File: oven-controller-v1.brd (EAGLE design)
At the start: 160 x 100 mm, 21 parts, among them Q1 IRFL310, U1 ARDUINO_SHIELDLONGPADS

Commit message: All parts on the board, cleaned up layout.
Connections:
- net 5V: now also U1.5V
- net A0: now also U1.A0
- net A1: now also U1.A1
- net A2: now also U1.A2
- net A3: now also U1.A3
- net CS_PIN10: now also U1.D10
- net CS_PIN5: now also U1.D5
- net CS_PIN6: now also U1.D6
- net CS_PIN7: now also U1.D7
- net CS_PIN8: now also U1.D8
- net CS_PIN9: now also U1.D9
- net GND: now also U1.GND@0, U1.GND@1, U1.GND@2
- net PIN12: now also U1.D12
- net SCLK_PIN4: now also U1.D4
- net SDA_PIN3: now also U1.D3
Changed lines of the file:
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@@
 <contactref element="ROTATESW" pad="4"/>
 <contactref element="LED1" pad="K"/>
-<wire x1="-71.12" y1="80.01" x2="-74.93" y2="-4.826" width="0" layer="19" extent="1-1"/>
+<contactref element="U1" pad="GND@2"/>
+<contactref element="U1" pad="GND@1"/>
+<contactref element="U1" pad="GND@0"/>
+<wire x1="25.654" y1="50.8" x2="28.194" y2="50.8" width="0" layer="19" extent="1-1"/>
+<wire x1="42.164" y1="2.54" x2="28.194" y2="50.8" width="0" layer="19" extent="1-1"/>
+<wire x1="-16.51" y1="82.55" x2="25.654" y2="50.8" width="0" layer="19" extent="1-1"/>
+<wire x1="-22.86" y1="88.9" x2="-16.51" y2="82.55" width="0" layer="19" extent="1-1"/>
+<wire x1="-22.86" y1="95.25" x2="-22.86" y2="88.9" width="0" layer="19" extent="1-1"/>
+<wire x1="-39.37" y1="95.25" x2="-22.86" y2="95.25" width="0" layer="19" extent="1-1"/>
+<wire x1="-39.37" y1="88.9" x2="-39.37" y2="95.25" width="0" layer="19" extent="1-1"/>
+<wire x1="-55.88" y1="88.9" x2="-39.37" y2="88.9" width="0" layer="19" extent="1-1"/>
+<wire x1="-58.42" y1="80.01" x2="-55.88" y2="88.9" width="0" layer="19" extent="1-1"/>
+<wire x1="-71.12" y1="80.01" x2="-58.42" y2="80.01" width="0" layer="19" extent="1-1"/>
 <wire x1="-72.39" y1="88.9" x2="-71.12" y2="80.01" width="0" layer="19" extent="1-1"/>
 <wire x1="-76.2" y1="95.25" x2="-72.39" y2="88.9" width="0" layer="19" extent="1-1"/>
-<wire x1="-58.42" y1="80.01" x2="-71.12" y2="80.01" width="0" layer="19" extent="1-1"/>
-<wire x1="-55.88" y1="88.9" x2="-58.42" y2="80.01" width="0" layer="19" extent="1-1"/>
-<wire x1="-39.37" y1="88.9" x2="-55.88" y2="88.9" width="0" layer="19" extent="1-1"/>
-<wire x1="-39.37" y1="95.25" x2="-39.37" y2="88.9" width="0" layer="19" extent="1-1"/>
-<wire x1="-22.86" y1="95.25" x2="-39.37" y2="95.25" width="0" layer="19" extent="1-1"/>
-<wire x1="-22.86" y1="88.9" x2="-22.86" y2="95.25" width="0" layer="19" extent="1-1"/>
-<wire x1="-16.51" y1="82.55" x2="-22.86" y2="88.9" width="0" layer="19" extent="1-1"/>
+<wire x1="-74.93" y1="-4.826" x2="-71.12" y2="80.01" width="0" layer="19" extent="1-1"/>
 </signal>
 <signal name="PIN12">
+<contactref element="U1" pad="D12"/>
 <contactref element="R2" pad="2"/>
 <contactref element="R1" pad="2"/>
 <wire x1="-63.5" y1="95.25" x2="-48.26" y2="95.25" width="0" layer="19" extent="1-1"/>
+<wire x1="37.084" y1="2.54" x2="-48.26" y2="95.25" width="0" layer="19" extent="1-1"/>
 </signal>
 <signal name="N$2">
@@
 <contactref element="SENSE5" pad="4"/>
 <contactref element="SENSE6" pad="4"/>
+<contactref element="U1" pad="D3"/>
 <wire x1="-20.32" y1="88.646" x2="-20.32" y2="94.996" width="0" layer="19" extent="1-1"/>
 <wire x1="-36.83" y1="94.996" x2="-20.32" y2="94.996" width="0" layer="19" extent="1-1"/>
@@
 <wire x1="-53.34" y1="88.646" x2="-36.83" y2="88.646" width="0" layer="19" extent="1-1"/>
 <wire x1="-69.85" y1="88.646" x2="-53.34" y2="88.646" width="0" layer="19" extent="1-1"/>
+<wire x1="12.954" y1="2.54" x2="-20.32" y2="88.646" width="0" layer="19" extent="1-1"/>
 </signal>
 <signal name="SCLK_PIN4">
@@
 <contactref element="SENSE5" pad="6"/>
 <contactref element="SENSE6" pad="6"/>
+<contactref element="U1" pad="D4"/>
 <wire x1="-15.24" y1="88.646" x2="-15.24" y2="94.996" width="0" layer="19" extent="1-1"/>
 <wire x1="-31.75" y1="94.996" x2="-15.24" y2="94.996" width="0" layer="19" extent="1-1"/>
@@
 <wire x1="-48.26" y1="88.646" x2="-31.75" y2="88.646" width="0" layer="19" extent="1-1"/>
 <wire x1="-64.77" y1="88.646" x2="-48.26" y2="88.646" width="0" layer="19" extent="1-1"/>
+<wire x1="15.494" y1="2.54" x2="-15.24" y2="88.646" width="0" layer="19" extent="1-1"/>
 </signal>
 <signal name="CS_PIN10">
 <contactref element="SENSE6" pad="5"/>
+<contactref element="U1" pad="D10"/>
+<wire x1="32.004" y1="2.54" x2="-34.29" y2="95.25" width="0" layer="19" extent="1-1"/>
 </signal>
 <signal name="N$1">
@@
 <signal name="CS_PIN6">
 <contactref element="SENSE2" pad="5"/>
+<contactref element="U1" pad="D6"/>
+<wire x1="20.574" y1="2.54" x2="-34.29" y2="88.9" width="0" layer="19" extent="1-1"/>
 </signal>
 <signal name="CS_PIN8">
 <contactref element="SENSE4" pad="5"/>
+<contactref element="U1" pad="D8"/>
+<wire x1="-67.31" y1="88.9" x2="26.924" y2="2.54" width="0" layer="19" extent="1-1"/>
 </signal>
 <signal name="CS_PIN7">
 <contactref element="SENSE3" pad="5"/>
+<contactref element="U1" pad="D7"/>
+<wire x1="23.114" y1="2.54" x2="-50.8" y2="88.9" width="0" layer="19" extent="1-1"/>
 </signal>
 <signal name="CS_PIN9">
 <contactref element="SENSE5" pad="5"/>
+<contactref element="U1" pad="D9"/>
+<wire x1="29.464" y1="2.54" x2="-17.78" y2="95.25" width="0" layer="19" extent="1-1"/>
 </signal>
 <signal name="CS_PIN5">
 <contactref element="SENSE1" pad="5"/>
+<contactref element="U1" pad="D5"/>
+<wire x1="18.034" y1="2.54" x2="-17.78" y2="88.9" width="0" layer="19" extent="1-1"/>
 </signal>
 <signal name="N$11">
@@
 <contactref element="R4" pad="1"/>
 <contactref element="JP1" pad="1"/>
-<wire x1="-36.83" y1="100.33" x2="-82.677" y2="-24.13" width="0" layer="19" extent="1-1"/>
+<contactref element="U1" pad="A0"/>
+<wire x1="18.034" y1="50.8" x2="-82.677" y2="-24.13" width="0" layer="19" extent="1-1"/>
+<wire x1="-36.83" y1="100.33" x2="18.034" y2="50.8" width="0" layer="19" extent="1-1"/>
 </signal>
 <signal name="N$10">
@@
 <contactref element="ROTATESW" pad="1"/>
 <contactref element="R10" pad="1"/>
+<contactref element="U1" pad="A1"/>
 <wire x1="-82.55" y1="-4.572" x2="-83.058" y2="-19.304" width="0" layer="19" extent="1-1"/>
+<wire x1="15.494" y1="50.8" x2="-82.55" y2="-4.572" width="0" layer="19" extent="1-1"/>
 </signal>
 <signal name="A2">
 <contactref element="ROTATESW" pad="2"/>
 <contactref element="R9" pad="1"/>
+<contactref element="U1" pad="A2"/>
 <wire x1="-80.01" y1="-4.826" x2="-83.058" y2="-14.732" width="0" layer="19" extent="1-1"/>
+<wire x1="12.954" y1="50.8" x2="-80.01" y2="-4.826" width="0" layer="19" extent="1-1"/>
 </signal>
 <signal name="A3">
 <contactref element="ROTATESW" pad="3"/>
 <contactref element="R8" pad="1"/>
+<contactref element="U1" pad="A3"/>
 <wire x1="-77.47" y1="-4.572" x2="-83.058" y2="-10.16" width="0" layer="19" extent="1-1"/>
+<wire x1="10.414" y1="50.8" x2="-77.47" y2="-4.572" width="0" layer="19" extent="1-1"/>
 </signal>
 <signal name="5V">
@@
 <contactref element="R4" pad="2"/>
 <contactref element="R3" pad="2"/>
+<contactref element="U1" pad="5V"/>
 <wire x1="-72.898" y1="-14.732" x2="-72.898" y2="-19.304" width="0" layer="19" extent="1-1"/>
 <wire x1="-72.898" y1="-10.16" x2="-72.898" y2="-14.732" width="0" layer="19" extent="1-1"/>
@@
 <wire x1="-27.94" y1="88.9" x2="-27.94" y2="95.25" width="0" layer="19" extent="1-1"/>
 <wire x1="-13.97" y1="100.33" x2="-26.67" y2="100.33" width="0" layer="19" extent="1-1"/>
+<wire x1="30.734" y1="50.8" x2="-13.97" y2="100.33" width="0" layer="19" extent="1-1"/>
 </signal>
 <signal name="VIN">

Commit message: Schematic and layout done. Connections to Arduino will have to be female headers because we don't have plated vias.
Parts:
- removed JP1: (no value), SparkFun-Connectors:1X02_LOCK_LONGPADS
- added 12VIN, START: (no value), SparkFun-Connectors:SCREWTERMINAL-3.5MM-2_LOCK
- LED2: value GREEN -> RED
- R2: value (none) -> 10k
- RELAY: device SparkFun-Connectors:1X02_LOCK_LONGPADS -> SparkFun-Connectors:SCREWTERMINAL-3.5MM-2_LOCK
- moved RELAY 158.3 mm to (55.9, 18.5), turned to 90 degrees
- moved R2 141.7 mm to (45.5, 13.0), turned to 135 degrees
- moved LED2 128.5 mm to (52.6, 50.3), turned to 90 degrees
- moved SENSE4 121.5 mm to (24.6, 23.1), turned to 270 degrees
- moved R10 118.5 mm to (25.1, 39.1)
- moved R1 118.2 mm to (42.2, 27.4), turned to 270 degrees
- moved R9 114.4 mm to (25.1, 34.8)
- moved R8 110.7 mm to (25.1, 30.0)
- moved ROTATESW 109.3 mm to (15.0, 44.7), turned to 180 degrees
- moved SENSE6 108.9 mm to (37.1, 23.1), turned to 270 degrees
- moved D1 108.5 mm to (49.3, 19.3), turned to 90 degrees
- moved LED1 108.1 mm to (44.2, 50.3), turned to 90 degrees
- moved SENSE3 103.0 mm to (18.3, 23.1), turned to 270 degrees
- moved SENSE5 93.1 mm to (31.0, 23.1), turned to 270 degrees
- moved Q1 87.8 mm to (52.1, 33.5)
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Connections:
- removed net N$1: SENSE2.2
- removed net N$4: SENSE1.2
- removed net N$5: SENSE3.2
- removed net N$6: SENSE4.2
- removed net N$8: SENSE5.2
- removed net N$9: SENSE6.2
- net A0: now also START.1; no longer JP1.1
- net GND: now also 12VIN.2
- net N$10: now also START.2; no longer JP1.2
- net VIN: now also 12VIN.1
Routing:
- net 5V: track 0.00 -> 62.7 mm
- net A0: track 0.00 -> 55.9 mm
- net SDA_PIN3: track 0.00 -> 46.9 mm
- net SCLK_PIN4: track 0.00 -> 40.8 mm
- net CS_PIN5: track 0.00 -> 31.6 mm
- net A3: track 0.00 -> 25.2 mm
- net PIN12: track 0.00 -> 21.2 mm
- net A2: track 0.00 -> 20.4 mm
- net VIN: track 0.00 -> 17.3 mm
- net A1: track 0.00 -> 15.3 mm
- net N$3: track 0.00 -> 15.3 mm
- net CS_PIN6: track 0.00 -> 13.9 mm
- net CS_PIN10: track 0.00 -> 13.7 mm
- net CS_PIN9: track 0.00 -> 13.3 mm
- net CS_PIN7: track 0.00 -> 12.4 mm
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- added copper zone on layer 16, net GND
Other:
- board size 160 x 100 mm -> 159.5 x 103.6 mm

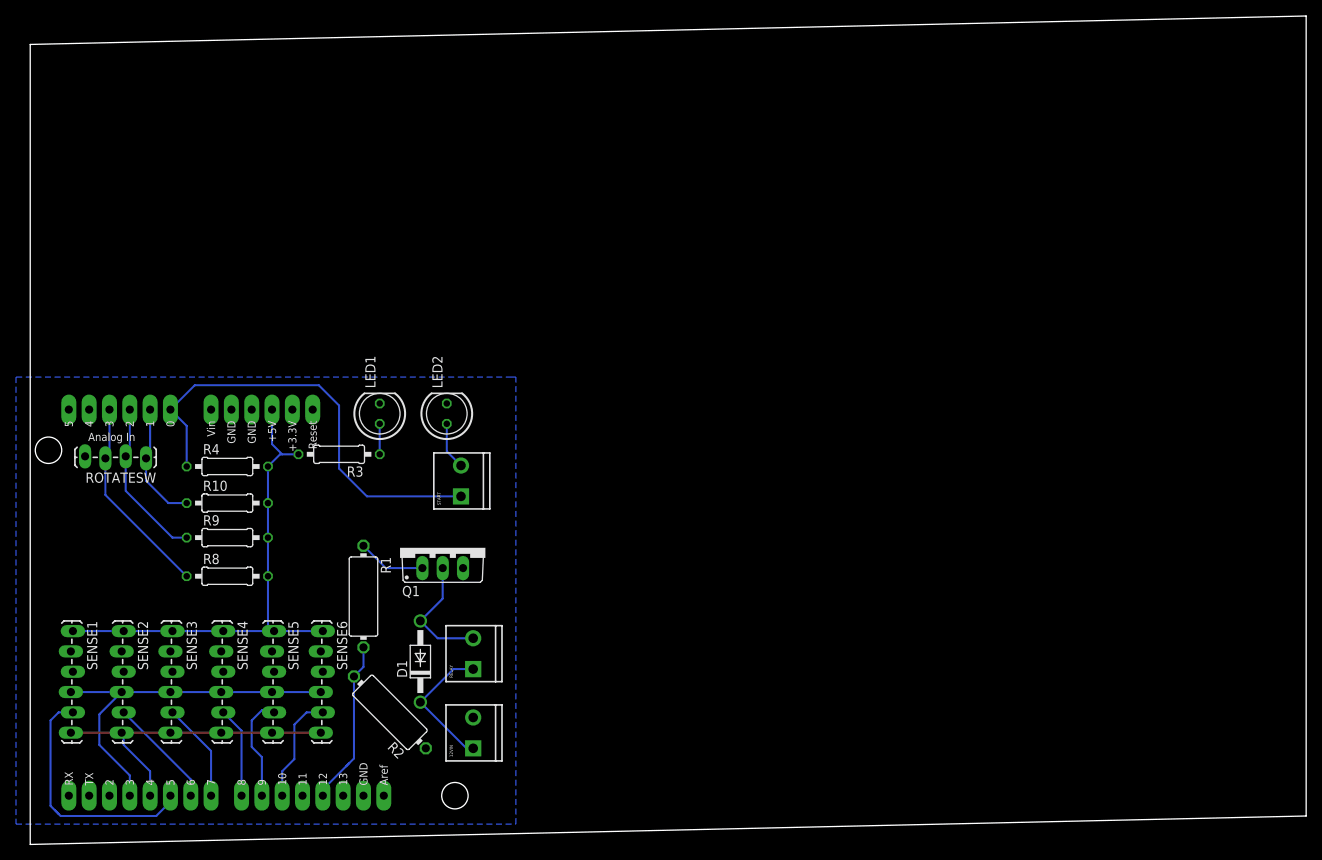
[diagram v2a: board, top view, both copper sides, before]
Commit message: Dimensions and spacing fixes.
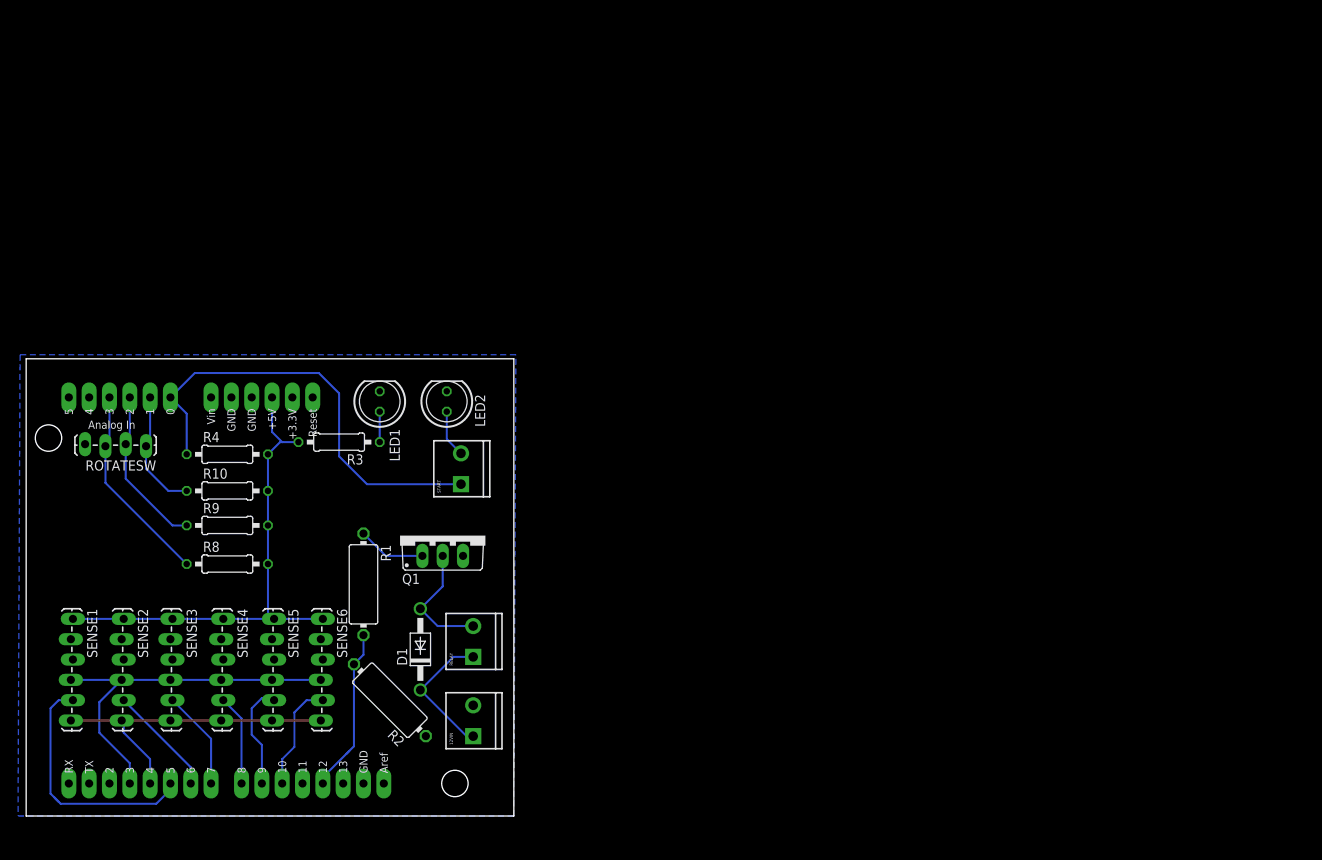
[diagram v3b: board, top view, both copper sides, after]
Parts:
- moved 12VIN 1.52 mm to (55.9, 10.2)
- moved D1 1.52 mm to (49.3, 20.8)
- moved LED1 1.52 mm to (44.2, 51.8)
- moved LED2 1.52 mm to (52.6, 51.8)
- moved Q1 1.52 mm to (52.1, 35.1)
- moved R1 1.52 mm to (42.2, 29.0)
- moved R10 1.52 mm to (25.1, 40.6)
- moved R4 1.52 mm to (25.1, 45.2)
- moved R9 1.52 mm to (25.1, 36.3)
- moved ROTATESW 1.52 mm to (15.0, 46.2)
- moved SENSE1 1.52 mm to (5.84, 24.6)
- moved SENSE2 1.52 mm to (12.2, 24.6)
- moved SENSE3 1.52 mm to (18.3, 24.6)
- moved SENSE4 1.52 mm to (24.6, 24.6)
- moved SENSE5 1.52 mm to (31.0, 24.6)
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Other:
- board size 159.5 x 103.6 mm -> 61 x 57.1 mm
